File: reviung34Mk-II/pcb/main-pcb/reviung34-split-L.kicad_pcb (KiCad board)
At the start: 2 copper layers, 202.7 x 100.1 mm, 92 parts, among them J1 8P8C, J2 8P8C, SW1 SW_PUSH, SW10 SW_PUSH, SW11 SW_PUSH, SW12 SW_PUSH, SW13 SW_PUSH, SW14 SW_PUSH, SW15 SW_PUSH, SW16 SW_PUSH, SW17 SW_PUSH, SW18 SW_PUSH, SW19 SW_PUSH, SW2 SW_PUSH, SW20 SW_PUSH, SW21 SW_PUSH, SW22 SW_PUSH, SW23 SW_PUSH, SW24 SW_PUSH, SW25 SW_PUSH, SW26 SW_PUSH, SW27 SW_PUSH, SW28 SW_PUSH, SW29 SW_PUSH, SW3 SW_PUSH, SW30 SW_PUSH, SW31 SW_PUSH, SW32 SW_PUSH, SW33 SW_PUSH, SW34 SW_PUSH, SW35 SW_PUSH, SW4 SW_PUSH, SW5 SW_PUSH, SW6 SW_PUSH, SW7 SW_PUSH, SW8 SW_PUSH, SW9 SW_PUSH, U1 ProMicro_r

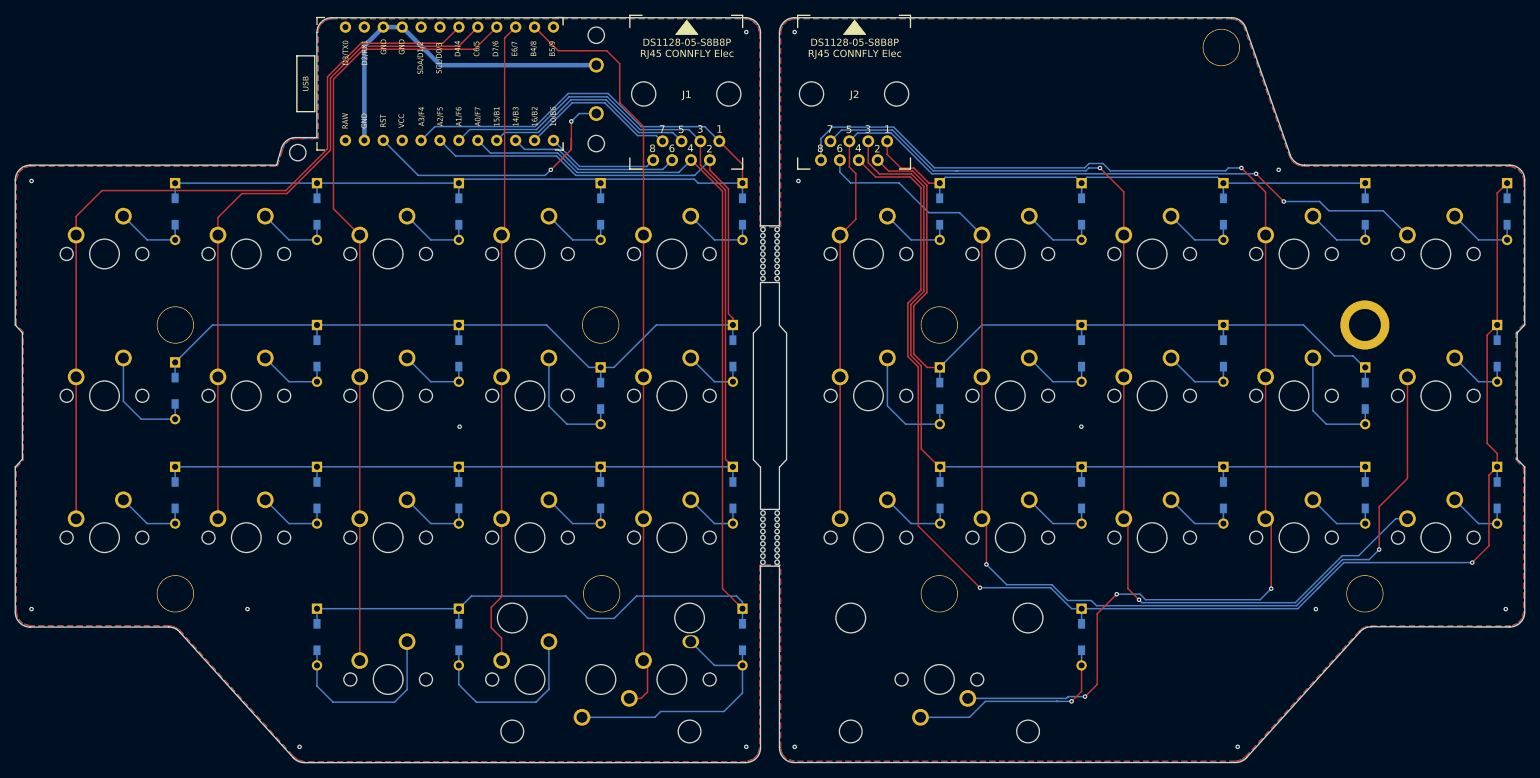
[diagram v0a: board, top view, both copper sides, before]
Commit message: Modified to use Kailh hotswaps
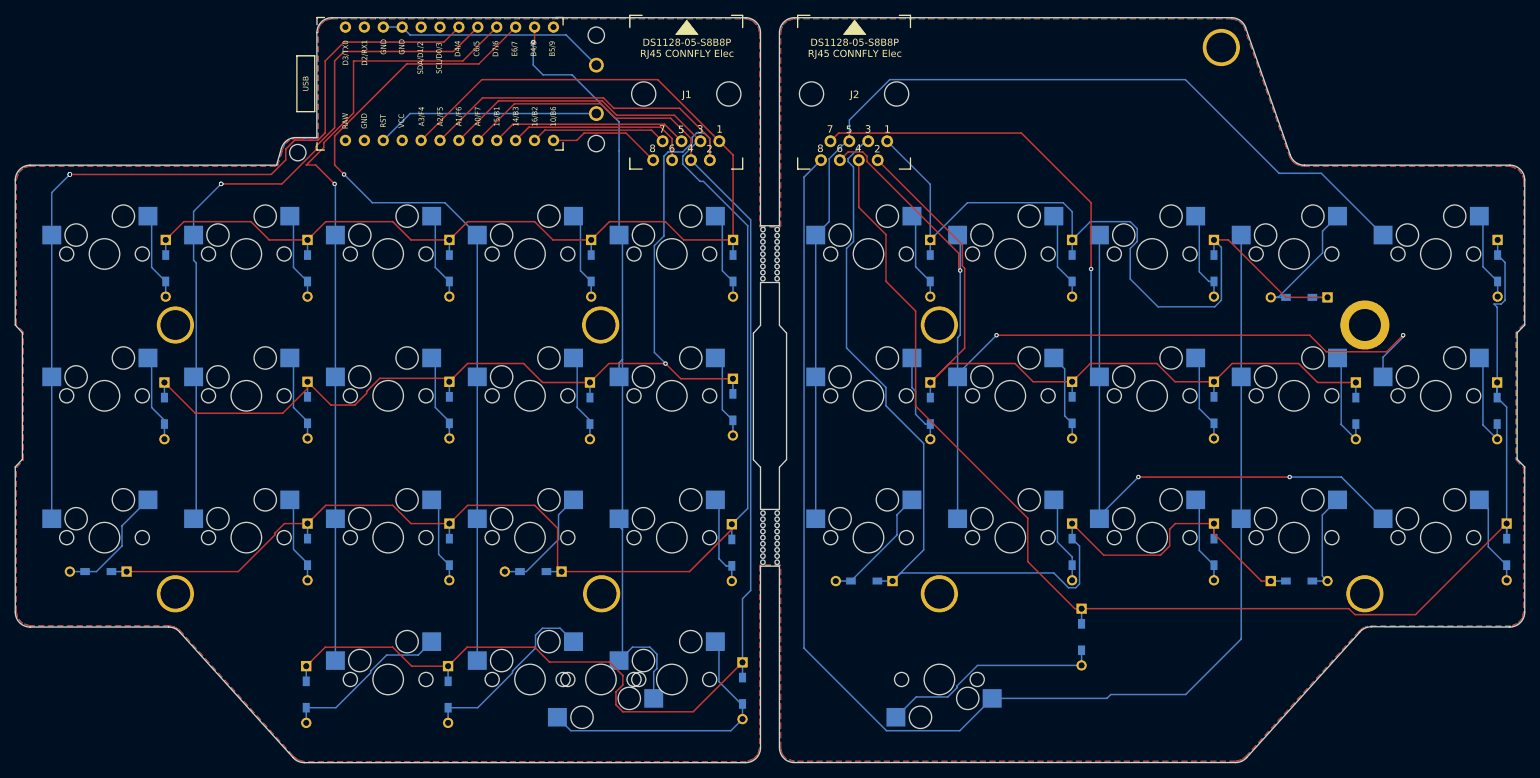
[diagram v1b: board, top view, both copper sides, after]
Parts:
- removed G***: LOGO, _reviung-kbd:R-x4-ver1
- removed G***: LOGO, _reviung-kbd:QMK-x4-ver1
- removed G***: LOGO, _reviung-kbd:REVIUNG34-split-PCB-logo
- H1, H10, H12, H2, H3, H4, H8, H9: footprint _reviung-kbd:HOLE -> kbd:M2_Hole_TH_Outside
- SW1, SW10, SW11, SW12, SW13, SW14, SW15, SW16, SW19, SW2, SW20, SW21, SW22, SW23, SW24, SW25, SW26, SW27, SW28, SW29, SW3, SW30, SW31, SW32, SW33, SW4, SW5, SW6, SW7, SW8, SW9: footprint _reviung-kbd:MXOnly-1U-NoLED -> kbd:CherryMX_Hotswap
- SW17: footprint _reviung-kbd:MXOnly-1U-5pinRcut -> kbd:CherryMX_Hotswap
- SW18: footprint _reviung-kbd:MXOnly-1U-5pinLcut -> kbd:CherryMX_Hotswap
- SW34, SW35: footprint _reviung-kbd:MXOnly-2U-NoLED -> kbd:CherryMX_Hotswap
- moved D27 15.4 mm to (163.8, 125.7), turned to 180 degrees
- moved D11 14.6 mm to (61.0, 124.5), turned to 180 degrees
- moved D22 14.6 mm to (222.2, 87.6), turned to 180 degrees
- moved D30 14.6 mm to (222.2, 125.7), turned to 0 degrees
- moved D14 13.7 mm to (119.4, 124.5), turned to 180 degrees
- moved D16 7.85 mm to (88.9, 141.0)
- moved D17 7.85 mm to (108.0, 141.0)
- moved D1 7.73 mm to (70.0, 83.7)
- moved D2 7.73 mm to (89.1, 83.7)
- moved D20 7.73 mm to (191.8, 83.7)
- moved D21 7.73 mm to (210.8, 83.7)
- moved D31 7.73 mm to (248.9, 83.7)
- moved D5 7.73 mm to (146.2, 83.7)
- moved D3 7.73 mm to (108.1, 83.7)
- moved D4 7.73 mm to (127.2, 83.7)
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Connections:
- U1 pad 1: (no net) -> Net-(U1-Pad1)
- U1 pad 12: (no net) -> Net-(U1-Pad12)
- U1 pad 2: (no net) -> Net-(U1-Pad2)
- U1 pad 21: (no net) -> VCC
- U1 pad 24: (no net) -> Net-(U1-Pad24)
- U1 pad 5: (no net) -> Net-(U1-Pad5)
- U1 pad 6: (no net) -> Net-(U1-Pad6)
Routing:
- net row2: track 168.3 -> 201.4 mm
- net row10: track 77.1 -> 107.6 mm
- net col3: track 87.0 -> 114.5 mm, vias 0 -> 1
- net row1: track 154.5 -> 181.5 mm, vias 0 -> 1
- net row12: track 117.0 -> 143.9 mm
- net row3: track 162.0 -> 184.6 mm
- net col16: track 151.6 -> 134.2 mm, vias 2 -> 3
- net row13: track 200.7 -> 184.2 mm, vias 2 -> 0
- net GND: track 47.0 -> 30.7 mm, vias 15 -> 0
- net row0: track 140.0 -> 155.4 mm
- net col18: track 174.9 -> 189.2 mm, vias 4 -> 0
- net reset: track 37.7 -> 30.1 mm, vias 2 -> 0
- net col4: track 102.2 -> 109.1 mm, vias 0 -> 1
- net Net-(D22-Pad2): track 10.4 -> 17.2 mm
- net col0: track 108.2 -> 114.2 mm, vias 0 -> 3
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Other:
- board text removed: "REVIUNG34 SPLIT rev 2.0 Designed by gtips 2020"
